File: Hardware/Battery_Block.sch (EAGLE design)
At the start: 22 parts, among them U1 MCP73831, U2 EDISON_CONNECTOR_FULLMOUNTING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, U3 EDISON_CONNECTOR_FULLHEADER

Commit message: file cleanup
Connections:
- net N$1 renamed VIN
- net N$6 renamed VBAT
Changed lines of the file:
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@@
 </segment>
 </net>
-<net name="N$1" class="0">
+<net name="VIN" class="0">
 <segment>
 <pinref part="JP1" gate="G$1" pin="VCC"/>
@@
 </segment>
 </net>
-<net name="N$6" class="0">
+<net name="VBAT" class="0">
 <segment>
 <pinref part="U1" gate="G$1" pin="VBAT"/>
@@
 <wire x1="175.26" y1="111.76" x2="198.12" y2="111.76" width="0.1524" layer="91"/>
 <wire x1="175.26" y1="109.22" x2="175.26" y2="111.76" width="0.1524" layer="91"/>
+<junction x="175.26" y="111.76"/>
 </segment>
 </net>

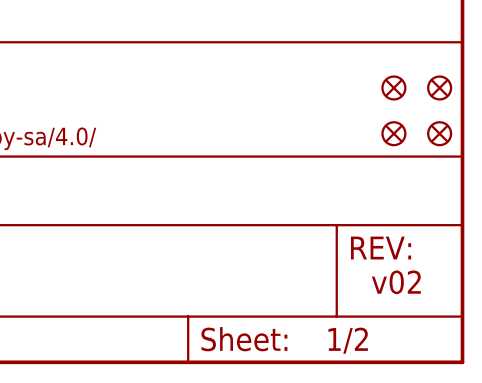
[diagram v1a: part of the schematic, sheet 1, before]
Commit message: Fix text rotation, go to v10
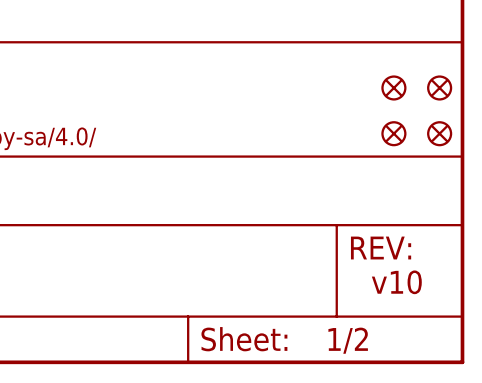
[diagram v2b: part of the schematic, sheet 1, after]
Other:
- note added: "v10"
- note removed: "v02"
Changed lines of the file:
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@@
 <?xml version="1.0" encoding="utf-8"?>
 <!DOCTYPE eagle SYSTEM "eagle.dtd">
-<eagle version="6.5.0">
+<eagle version="6.6.0">
 <drawing>
 <settings>
@@
 <layer number="254" name="cooling" color="7" fill="1" visible="yes" active="yes"/>
 </layers>
-<schematic xreflabel="%F%N/%S" xrefpart="1_/%S.%C%R">
+<schematic xreflabel="%F%N/%S" xrefpart="/%S.%C%R">
 <attributes>
 </attributes>
@@
 <plain>
 <text x="167.64" y="10.16" size="2.54" layer="94">Casey Kuhns</text>
-<text x="238.76" y="7.62" size="2.54" layer="94">v02</text>
+<text x="238.76" y="7.62" size="2.54" layer="94">v10</text>
 </plain>
 <instances>

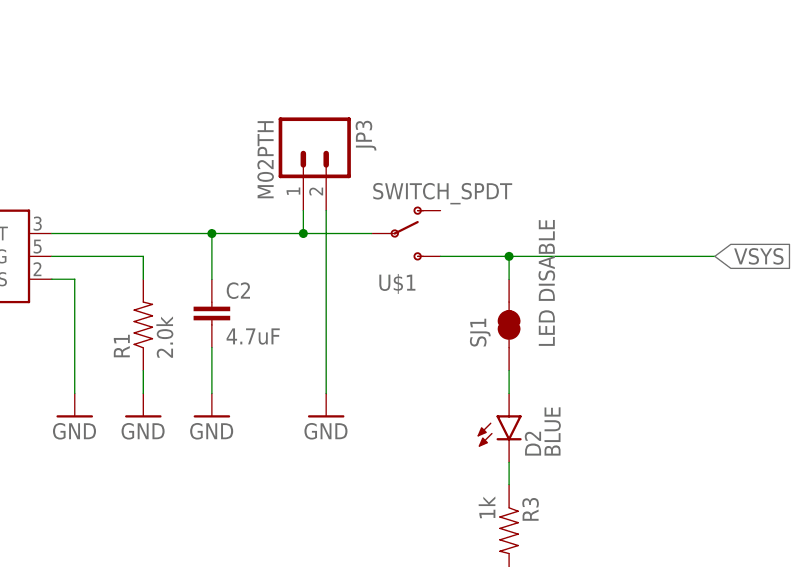
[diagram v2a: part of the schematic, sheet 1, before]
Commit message: Add some silk, update fp, ready for reds
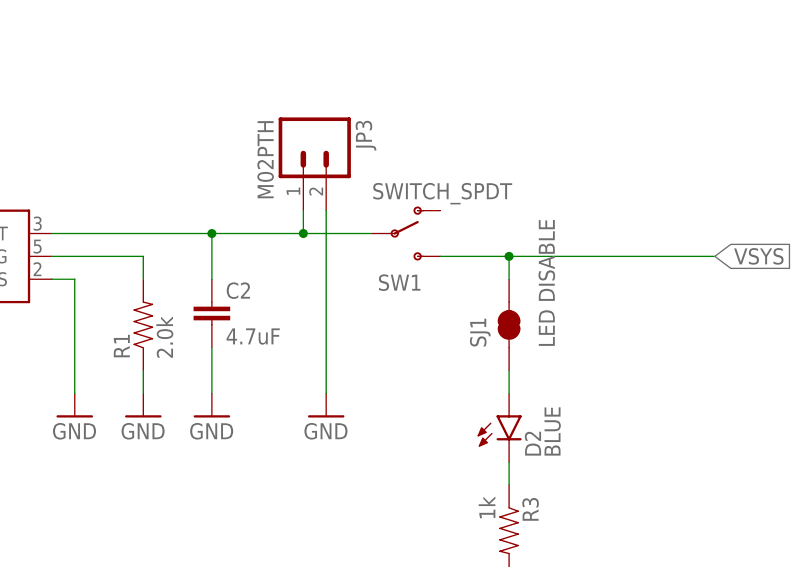
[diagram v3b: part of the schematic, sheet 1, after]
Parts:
- renumbered U$1 to SW1
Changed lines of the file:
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@@
 <grid distance="0.1" unitdist="inch" unit="inch" style="lines" multiple="1" display="no" altdistance="0.01" altunitdist="inch" altunit="inch"/>
 <layers>
-<layer number="1" name="Top" color="4" fill="1" visible="no" active="no"/>
-<layer number="2" name="Route2" color="1" fill="3" visible="no" active="no"/>
-<layer number="3" name="Route3" color="4" fill="3" visible="no" active="no"/>
-<layer number="4" name="Route4" color="1" fill="4" visible="no" active="no"/>
-<layer number="5" name="Route5" color="4" fill="4" visible="no" active="no"/>
-<layer number="6" name="Route6" color="1" fill="8" visible="no" active="no"/>
-<layer number="7" name="Route7" color="4" fill="8" visible="no" active="no"/>
-<layer number="8" name="Route8" color="1" fill="2" visible="no" active="no"/>
-<layer number="9" name="Route9" color="4" fill="2" visible="no" active="no"/>
-<layer number="10" name="Route10" color="1" fill="7" visible="no" active="no"/>
-<layer number="11" name="Route11" color="4" fill="7" visible="no" active="no"/>
-<layer number="12" name="Route12" color="1" fill="5" visible="no" active="no"/>
-<layer number="13" name="Route13" color="4" fill="5" visible="no" active="no"/>
-<layer number="14" name="Route14" color="1" fill="6" visible="no" active="no"/>
-<layer number="15" name="Route15" color="4" fill="6" visible="no" active="no"/>
-<layer number="16" name="Bottom" color="1" fill="1" visible="no" active="no"/>
-<layer number="17" name="Pads" color="2" fill="1" visible="no" active="no"/>
-<layer number="18" name="Vias" color="2" fill="1" visible="no" active="no"/>
-<layer number="19" name="Unrouted" color="6" fill="1" visible="no" active="no"/>
-<layer number="20" name="Dimension" color="15" fill="1" visible="no" active="no"/>
-<layer number="21" name="tPlace" color="7" fill="1" visible="no" active="no"/>
-<layer number="22" name="bPlace" color="7" fill="1" visible="no" active="no"/>
-<layer number="23" name="tOrigins" color="15" fill="1" visible="no" active="no"/>
-<layer number="24" name="bOrigins" color="15" fill="1" visible="no" active="no"/>
-<layer number="25" name="tNames" color="7" fill="1" visible="no" active="no"/>
-<layer number="26" name="bNames" color="7" fill="1" visible="no" active="no"/>
-<layer number="27" name="tValues" color="7" fill="1" visible="no" active="no"/>
-<layer number="28" name="bValues" color="7" fill="1" visible="no" active="no"/>
+<layer number="1" name="Top" color="4" fill="1" visible="yes" active="no"/>
+<layer number="2" name="Route2" color="1" fill="3" visible="yes" active="no"/>
+<layer number="3" name="Route3" color="4" fill="3" visible="yes" active="no"/>
+<layer number="4" name="Route4" color="1" fill="4" visible="yes" active="no"/>
+<layer number="5" name="Route5" color="4" fill="4" visible="yes" active="no"/>
+<layer number="6" name="Route6" color="1" fill="8" visible="yes" active="no"/>
+<layer number="7" name="Route7" color="4" fill="8" visible="yes" active="no"/>
+<layer number="8" name="Route8" color="1" fill="2" visible="yes" active="no"/>
+<layer number="9" name="Route9" color="4" fill="2" visible="yes" active="no"/>
+<layer number="10" name="Route10" color="1" fill="7" visible="yes" active="no"/>
+<layer number="11" name="Route11" color="4" fill="7" visible="yes" active="no"/>
+<layer number="12" name="Route12" color="1" fill="5" visible="yes" active="no"/>
+<layer number="13" name="Route13" color="4" fill="5" visible="yes" active="no"/>
+<layer number="14" name="Route14" color="1" fill="6" visible="yes" active="no"/>
+<layer number="15" name="Route15" color="4" fill="6" visible="yes" active="no"/>
+<layer number="16" name="Bottom" color="1" fill="1" visible="yes" active="no"/>
+<layer number="17" name="Pads" color="2" fill="1" visible="yes" active="no"/>
+<layer number="18" name="Vias" color="2" fill="1" visible="yes" active="no"/>
+<layer number="19" name="Unrouted" color="6" fill="1" visible="yes" active="no"/>
+<layer number="20" name="Dimension" color="15" fill="1" visible="yes" active="no"/>
+<layer number="21" name="tPlace" color="16" fill="1" visible="yes" active="no"/>
+<layer number="22" name="bPlace" color="14" fill="1" visible="yes" active="no"/>
+<layer number="23" name="tOrigins" color="15" fill="1" visible="yes" active="no"/>
+<layer number="24" name="bOrigins" color="15" fill="1" visible="yes" active="no"/>
+<layer number="25" name="tNames" color="7" fill="1" visible="yes" active="no"/>
+<layer number="26" name="bNames" color="7" fill="1" visible="yes" active="no"/>
+<layer number="27" name="tValues" color="7" fill="1" visible="yes" active="no"/>
+<layer number="28" name="bValues" color="7" fill="1" visible="yes" active="no"/>
 <layer number="29" name="tStop" color="7" fill="3" visible="no" active="no"/>
 <layer number="30" name="bStop" color="7" fill="6" visible="no" active="no"/>
@@
 <layer number="35" name="tGlue" color="7" fill="4" visible="no" active="no"/>
 <layer number="36" name="bGlue" color="7" fill="5" visible="no" active="no"/>
-<layer number="37" name="tTest" color="7" fill="1" visible="no" active="no"/>
-<layer number="38" name="bTest" color="7" fill="1" visible="no" active="no"/>
+<layer number="37" name="tTest" color="7" fill="1" visible="yes" active="no"/>
+<layer number="38" name="bTest" color="7" fill="1" visible="yes" active="no"/>
 <layer number="39" name="tKeepout" color="4" fill="11" visible="no" active="no"/>
 <layer number="40" name="bKeepout" color="1" fill="11" visible="no" active="no"/>
@@
 <layer number="44" name="Drills" color="7" fill="1" visible="no" active="no"/>
 <layer number="45" name="Holes" color="7" fill="1" visible="no" active="no"/>
-<layer number="46" name="Milling" color="3" fill="1" visible="no" active="no"/>
-<layer number="47" name="Measures" color="7" fill="1" visible="no" active="no"/>
-<layer number="48" name="Document" color="7" fill="1" visible="no" active="no"/>
-<layer number="49" name="Reference" color="7" fill="1" visible="no" active="no"/>
-<layer number="50" name="dxf" color="7" fill="1" visible="no" active="no"/>
-<layer number="51" name="tDocu" color="7" fill="1" visible="no" active="no"/>
-<layer number="52" name="bDocu" color="7" fill="1" visible="no" active="no"/>
-<layer number="53" name="tGND_GNDA" color="7" fill="9" visible="no" active="no"/>
-<layer number="54" name="bGND_GNDA" color="1" fill="9" visible="no" active="no"/>
-<layer number="56" name="wert" color="7" fill="1" visible="no" active="no"/>
-<layer number="57" name="tCAD" color="7" fill="1" visible="no" active="no"/>
+<layer number="46" name="Milling" color="3" fill="1" visible="yes" active="no"/>
+<layer number="47" name="Measures" color="7" fill="1" visible="yes" active="no"/>
+<layer number="48" name="Document" color="7" fill="1" visible="yes" active="no"/>
+<layer number="49" name="Reference" color="7" fill="1" visible="yes" active="no"/>
+<layer number="50" name="dxf" color="7" fill="1" visible="yes" active="no"/>
+<layer number="51" name="tDocu" color="6" fill="1" visible="yes" active="no"/>
+<layer number="52" name="bDocu" color="7" fill="1" visible="yes" active="no"/>
+<layer number="53" name="tGND_GNDA" color="7" fill="9" visible="yes" active="no"/>
+<layer number="54" name="bGND_GNDA" color="1" fill="9" visible="yes" active="no"/>
+<layer number="56" name="wert" color="7" fill="1" visible="yes" active="no"/>
+<layer number="57" name="tCAD" color="7" fill="1" visible="yes" active="no"/>
 <layer number="91" name="Nets" color="2" fill="1" visible="yes" active="yes"/>
 <layer number="92" name="Busses" color="1" fill="1" visible="yes" active="yes"/>
@@
 <part name="GND2" library="SparkFun-Aesthetics" deviceset="GND" device=""/>
 <part name="C1" library="SparkFun-Capacitors" deviceset="4.7UF-6.3V-10%(0603)" device="0603" value="4.7uF"/>
-<part name="U$1" library="SparkFun-Electromechanical" deviceset="SWITCH_SPDT" device=""/>
+<part name="SW1" library="SparkFun-Electromechanical" deviceset="SWITCH_SPDT" device=""/>
 <part name="R1" library="SparkFun-Resistors" deviceset="2.0KOHM1/10W5%(0603)" device="" value="2.0k"/>
 <part name="JP3" library="SparkFun-Connectors" deviceset="M02" device="PTH"/>
@@
 <instance part="GND2" gate="1" x="55.88" y="93.98"/>
 <instance part="C1" gate="G$1" x="83.82" y="106.68"/>
-<instance part="U$1" gate="G$1" x="162.56" y="114.3"/>
+<instance part="SW1" gate="G$1" x="162.56" y="114.3"/>
 <instance part="R1" gate="G$1" x="134.62" y="104.14" rot="R90"/>
 <instance part="JP3" gate="G$1" x="152.4" y="124.46" rot="R270"/>
@@
 <wire x1="152.4" y1="114.3" x2="152.4" y2="116.84" width="0.1524" layer="91"/>
 <junction x="142.24" y="114.3"/>
-<pinref part="U$1" gate="G$1" pin="P"/>
+<pinref part="SW1" gate="G$1" pin="P"/>
 <wire x1="152.4" y1="114.3" x2="160.02" y2="114.3" width="0.1524" layer="91"/>
 <junction x="152.4" y="114.3"/>
@@
 <net name="VSYS" class="0">
 <segment>
-<pinref part="U$1" gate="G$1" pin="S"/>
+<pinref part="SW1" gate="G$1" pin="S"/>
 <wire x1="167.64" y1="111.76" x2="175.26" y2="111.76" width="0.1524" layer="91"/>
 <label x="198.12" y="111.76" size="1.778" layer="95" xref="yes"/>
